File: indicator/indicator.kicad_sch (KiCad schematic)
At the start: 18 parts, among them J1 Conn_01x07_Pin

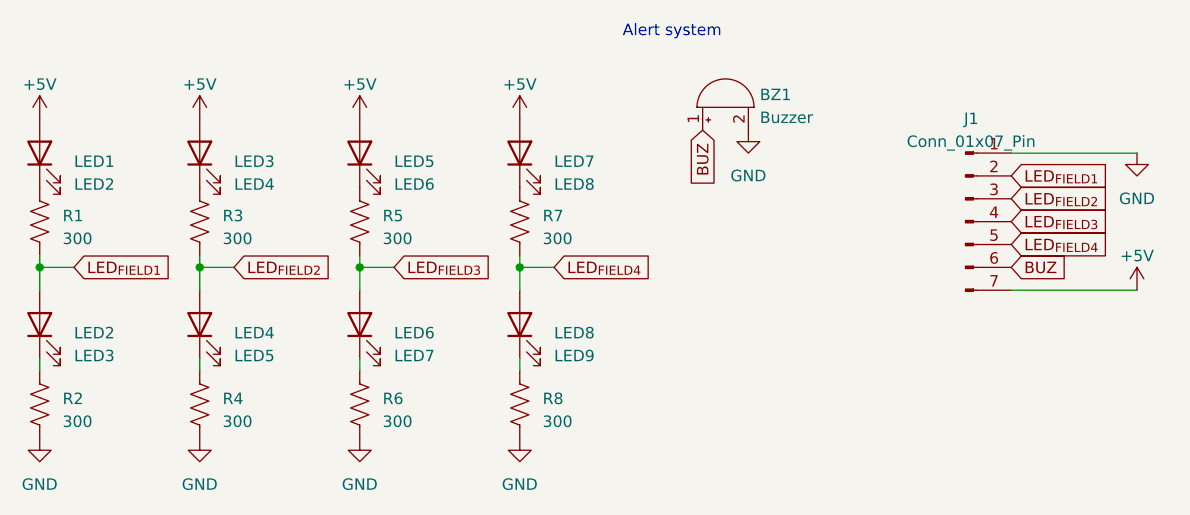
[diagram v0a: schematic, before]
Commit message: Changed indicator resistor values
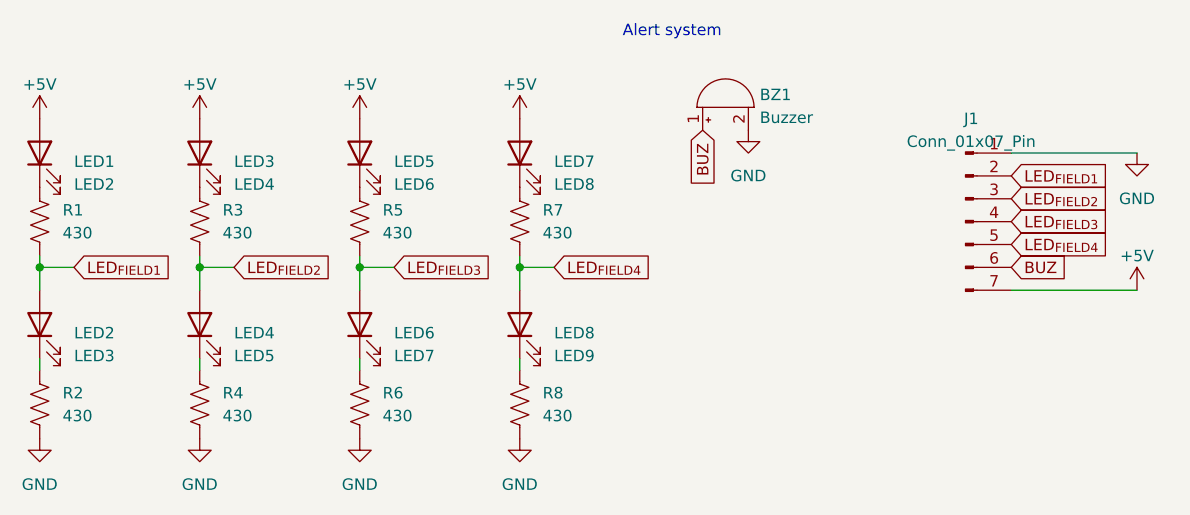
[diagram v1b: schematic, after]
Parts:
- R1, R2, R3, R4, R5, R6, R7, R8: value 300 -> 430
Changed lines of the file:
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@@
   (symbol (lib_id "Device:R_US") (at 121.92 114.3 180) (unit 1)
     (in_bom yes) (on_board yes) (dnp no) (fields_autoplaced)
-    (property "Reference" "R8" (at 124.46 113.665 0)
-      (effects (font (size 1.27 1.27)) (justify right))
-    )
-    (property "Value" "300" (at 124.46 116.205 0)
+    (property "Reference" "R8" (at 124.46 113.03 0)
+      (effects (font (size 1.27 1.27)) (justify right))
+    )
+    (property "Value" "430" (at 124.46 115.57 0)
       (effects (font (size 1.27 1.27)) (justify right))
     )
@@
     (pin "2")
     (instances
-      (project "AbdullahLEDboard"
+      (project "indicator"
         (path "/cede0fc5-7981-4758-9694-56d43565c74a"
           (reference "R8") (unit 1)
@@
     (pin "2")
     (instances
-      (project "AbdullahLEDboard"
+      (project "indicator"
         (path "/cede0fc5-7981-4758-9694-56d43565c74a"
           (reference "LED7") (unit 1)
@@
   (symbol (lib_id "Device:R_US") (at 104.14 114.3 180) (unit 1)
     (in_bom yes) (on_board yes) (dnp no) (fields_autoplaced)
-    (property "Reference" "R6" (at 106.68 113.665 0)
-      (effects (font (size 1.27 1.27)) (justify right))
-    )
-    (property "Value" "300" (at 106.68 116.205 0)
+    (property "Reference" "R6" (at 106.68 113.03 0)
+      (effects (font (size 1.27 1.27)) (justify right))
+    )
+    (property "Value" "430" (at 106.68 115.57 0)
       (effects (font (size 1.27 1.27)) (justify right))
     )
@@
     (pin "2")
     (instances
-      (project "AbdullahLEDboard"
+      (project "indicator"
         (path "/cede0fc5-7981-4758-9694-56d43565c74a"
           (reference "R6") (unit 1)
@@
     (pin "2")
     (instances
-      (project "AbdullahLEDboard"
+      (project "indicator"
         (path "/cede0fc5-7981-4758-9694-56d43565c74a"
           (reference "LED5") (unit 1)
@@
     (pin "1")
     (instances
-      (project "AbdullahLEDboard"
+      (project "indicator"
         (path "/cede0fc5-7981-4758-9694-56d43565c74a"
           (reference "#PWR07") (unit 1)
@@
   (symbol (lib_id "Device:R_US") (at 68.58 114.3 180) (unit 1)
     (in_bom yes) (on_board yes) (dnp no) (fields_autoplaced)
-    (property "Reference" "R2" (at 71.12 113.665 0)
-      (effects (font (size 1.27 1.27)) (justify right))
-    )
-    (property "Value" "300" (at 71.12 116.205 0)
+    (property "Reference" "R2" (at 71.12 113.03 0)
+      (effects (font (size 1.27 1.27)) (justify right))
+    )
+    (property "Value" "430" (at 71.12 115.57 0)
       (effects (font (size 1.27 1.27)) (justify right))
     )
@@
     (pin "2")
     (instances
-      (project "AbdullahLEDboard"
+      (project "indicator"
         (path "/cede0fc5-7981-4758-9694-56d43565c74a"
           (reference "R2") (unit 1)
@@
     (pin "2")
     (instances
-      (project "AbdullahLEDboard"
+      (project "indicator"
         (path "/cede0fc5-7981-4758-9694-56d43565c74a"
           (reference "BZ1") (unit 1)
@@
     (pin "2")
     (instances
-      (project "AbdullahLEDboard"
+      (project "indicator"
         (path "/cede0fc5-7981-4758-9694-56d43565c74a"
           (reference "LED6") (unit 1)
@@
     (pin "2")
     (instances
-      (project "AbdullahLEDboard"
+      (project "indicator"
         (path "/cede0fc5-7981-4758-9694-56d43565c74a"
           (reference "LED2") (unit 1)
@@
     (pin "1")
     (instances
-      (project "AbdullahLEDboard"
+      (project "indicator"
         (path "/cede0fc5-7981-4758-9694-56d43565c74a"
           (reference "#PWR05") (unit 1)
@@
     (pin "1")
     (instances
-      (project "AbdullahLEDboard"
+      (project "indicator"
         (path "/cede0fc5-7981-4758-9694-56d43565c74a"
           (reference "#PWR012") (unit 1)
@@
     (pin "2")
     (instances
-      (project "AbdullahLEDboard"
+      (project "indicator"
         (path "/cede0fc5-7981-4758-9694-56d43565c74a"
           (reference "LED8") (unit 1)
@@
     (pin "1")
     (instances
-      (project "AbdullahLEDboard"
+      (project "indicator"
         (path "/cede0fc5-7981-4758-9694-56d43565c74a"
           (reference "#PWR017") (unit 1)
@@
     (pin "1")
     (instances
-      (project "AbdullahLEDboard"
+      (project "indicator"
         (path "/cede0fc5-7981-4758-9694-56d43565c74a"
           (reference "#PWR011") (unit 1)
@@
     (pin "1")
     (instances
-      (project "AbdullahLEDboard"
+      (project "indicator"
         (path "/cede0fc5-7981-4758-9694-56d43565c74a"
           (reference "#PWR02") (unit 1)
@@
   (symbol (lib_id "Device:R_US") (at 68.58 93.98 180) (unit 1)
     (in_bom yes) (on_board yes) (dnp no) (fields_autoplaced)
-    (property "Reference" "R1" (at 71.12 93.345 0)
-      (effects (font (size 1.27 1.27)) (justify right))
-    )
-    (property "Value" "300" (at 71.12 95.885 0)
+    (property "Reference" "R1" (at 71.12 92.71 0)
+      (effects (font (size 1.27 1.27)) (justify right))
+    )
+    (property "Value" "430" (at 71.12 95.25 0)
       (effects (font (size 1.27 1.27)) (justify right))
     )
@@
     (pin "2")
     (instances
-      (project "AbdullahLEDboard"
+      (project "indicator"
         (path "/cede0fc5-7981-4758-9694-56d43565c74a"
           (reference "R1") (unit 1)
@@
   (symbol (lib_id "Device:R_US") (at 86.36 114.3 180) (unit 1)
     (in_bom yes) (on_board yes) (dnp no) (fields_autoplaced)
-    (property "Reference" "R4" (at 88.9 113.665 0)
-      (effects (font (size 1.27 1.27)) (justify right))
-    )
-    (property "Value" "300" (at 88.9 116.205 0)
+    (property "Reference" "R4" (at 88.9 113.03 0)
+      (effects (font (size 1.27 1.27)) (justify right))
+    )
+    (property "Value" "430" (at 88.9 115.57 0)
       (effects (font (size 1.27 1.27)) (justify right))
     )
@@
     (pin "2")
     (instances
-      (project "AbdullahLEDboard"
+      (project "indicator"
         (path "/cede0fc5-7981-4758-9694-56d43565c74a"
           (reference "R4") (unit 1)
@@
     (pin "1")
     (instances
-      (project "AbdullahLEDboard"
+      (project "indicator"
         (path "/cede0fc5-7981-4758-9694-56d43565c74a"
           (reference "#PWR03") (unit 1)
@@
     (pin "2")
     (instances
-      (project "AbdullahLEDboard"
+      (project "indicator"
         (path "/cede0fc5-7981-4758-9694-56d43565c74a"
           (reference "LED4") (unit 1)
@@
     (pin "1")
     (instances
-      (project "AbdullahLEDboard"
+      (project "indicator"
         (path "/cede0fc5-7981-4758-9694-56d43565c74a"
           (reference "#PWR08") (unit 1)
@@
   (symbol (lib_id "Device:R_US") (at 121.92 93.98 180) (unit 1)
     (in_bom yes) (on_board yes) (dnp no) (fields_autoplaced)
-    (property "Reference" "R7" (at 124.46 93.345 0)
-      (effects (font (size 1.27 1.27)) (justify right))
-    )
-    (property "Value" "300" (at 124.46 95.885 0)
+    (property "Reference" "R7" (at 124.46 92.71 0)
+      (effects (font (size 1.27 1.27)) (justify right))
+    )
+    (property "Value" "430" (at 124.46 95.25 0)
       (effects (font (size 1.27 1.27)) (justify right))
     )
@@
     (pin "2")
     (instances
-      (project "AbdullahLEDboard"
+      (project "indicator"
         (path "/cede0fc5-7981-4758-9694-56d43565c74a"
           (reference "R7") (unit 1)
@@
     (pin "2")
     (instances
-      (project "AbdullahLEDboard"
+      (project "indicator"
         (path "/cede0fc5-7981-4758-9694-56d43565c74a"
           (reference "LED1") (unit 1)
@@
     (pin "2")
     (instances
-      (project "AbdullahLEDboard"
+      (project "indicator"
         (path "/cede0fc5-7981-4758-9694-56d43565c74a"
           (reference "LED3") (unit 1)
@@
   (symbol (lib_id "Device:R_US") (at 86.36 93.98 180) (unit 1)
     (in_bom yes) (on_board yes) (dnp no) (fields_autoplaced)
-    (property "Reference" "R3" (at 88.9 93.345 0)
-      (effects (font (size 1.27 1.27)) (justify right))
-    )
-    (property "Value" "300" (at 88.9 95.885 0)
+    (property "Reference" "R3" (at 88.9 92.71 0)
+      (effects (font (size 1.27 1.27)) (justify right))
+    )
+    (property "Value" "430" (at 88.9 95.25 0)
       (effects (font (size 1.27 1.27)) (justify right))
     )
@@
     (pin "2")
     (instances
-      (project "AbdullahLEDboard"
+      (project "indicator"
         (path "/cede0fc5-7981-4758-9694-56d43565c74a"
           (reference "R3") (unit 1)
@@
     (pin "7")
     (instances
-      (project "AbdullahLEDboard"
+      (project "indicator"
         (path "/cede0fc5-7981-4758-9694-56d43565c74a"
           (reference "J1") (unit 1)
@@
     (pin "1")
     (instances
-      (project "AbdullahLEDboard"
+      (project "indicator"
         (path "/cede0fc5-7981-4758-9694-56d43565c74a"
           (reference "#PWR06") (unit 1)
@@
     (pin "1")
     (instances
-      (project "AbdullahLEDboard"
+      (project "indicator"
         (path "/cede0fc5-7981-4758-9694-56d43565c74a"
           (reference "#PWR01") (unit 1)
@@
     (pin "1")
     (instances
-      (project "AbdullahLEDboard"
+      (project "indicator"
         (path "/cede0fc5-7981-4758-9694-56d43565c74a"
           (reference "#PWR04") (unit 1)
@@
   (symbol (lib_id "Device:R_US") (at 104.14 93.98 180) (unit 1)
     (in_bom yes) (on_board yes) (dnp no) (fields_autoplaced)
-    (property "Reference" "R5" (at 106.68 93.345 0)
-      (effects (font (size 1.27 1.27)) (justify right))
-    )
-    (property "Value" "300" (at 106.68 95.885 0)
+    (property "Reference" "R5" (at 106.68 92.71 0)
+      (effects (font (size 1.27 1.27)) (justify right))
+    )
+    (property "Value" "430" (at 106.68 95.25 0)
       (effects (font (size 1.27 1.27)) (justify right))
     )
@@
     (pin "2")
     (instances
-      (project "AbdullahLEDboard"
+      (project "indicator"
         (path "/cede0fc5-7981-4758-9694-56d43565c74a"
           (reference "R5") (unit 1)
